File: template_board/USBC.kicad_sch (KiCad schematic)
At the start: 13 parts, among them J1 USB_C_Receptacle_USB2.0_16P, U1 IP4220CZ6, U11 FSUSB42UMX, U3 IP4220CZ6

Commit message: chamt skończony chyba
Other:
- moved on the sheet: C44, C45, C46, J1, R56, R57, R58, R59, R60, R61, U1, U11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

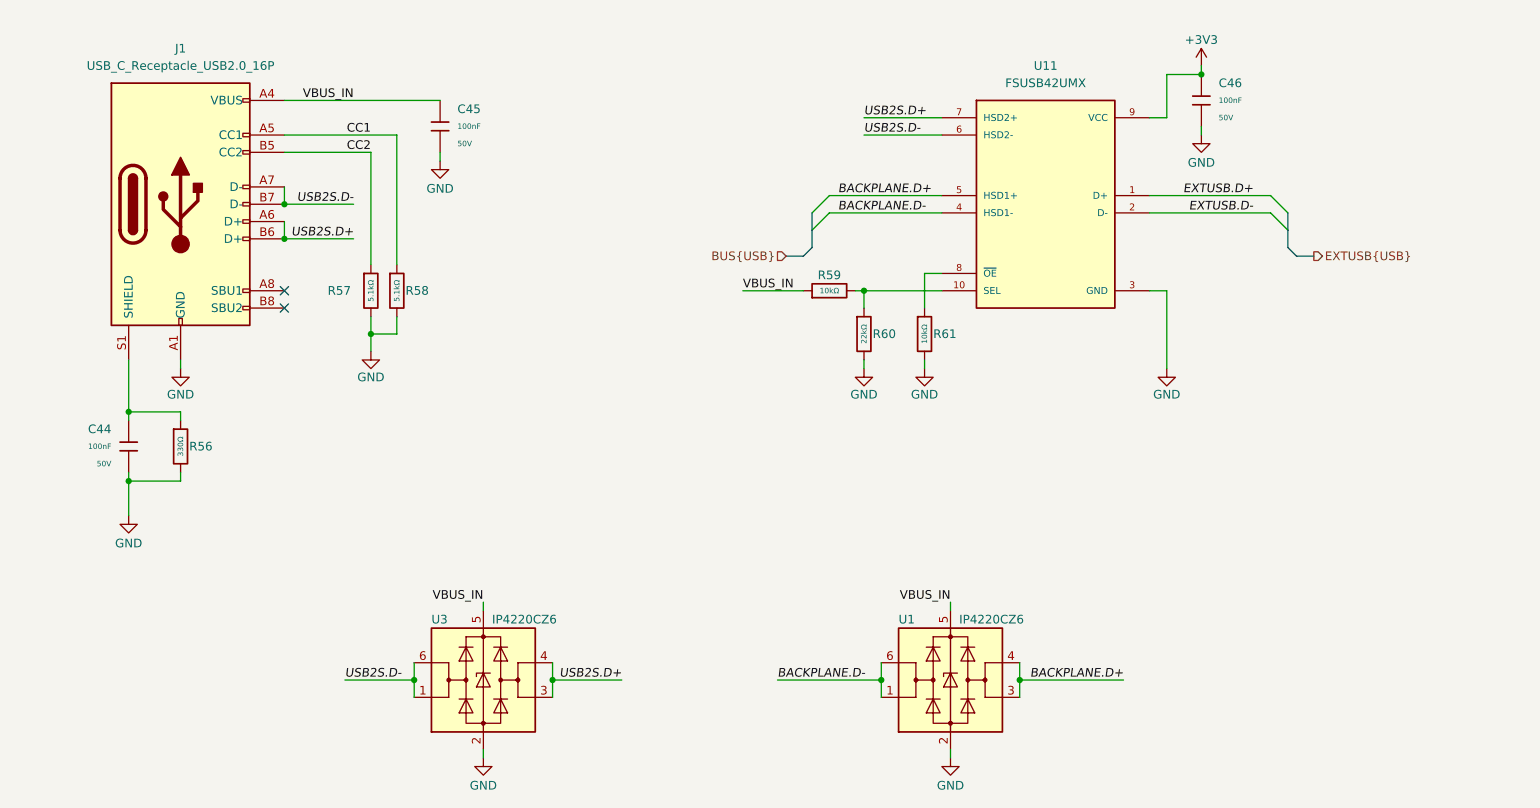
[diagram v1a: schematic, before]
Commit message: sub leyoyut partially completed
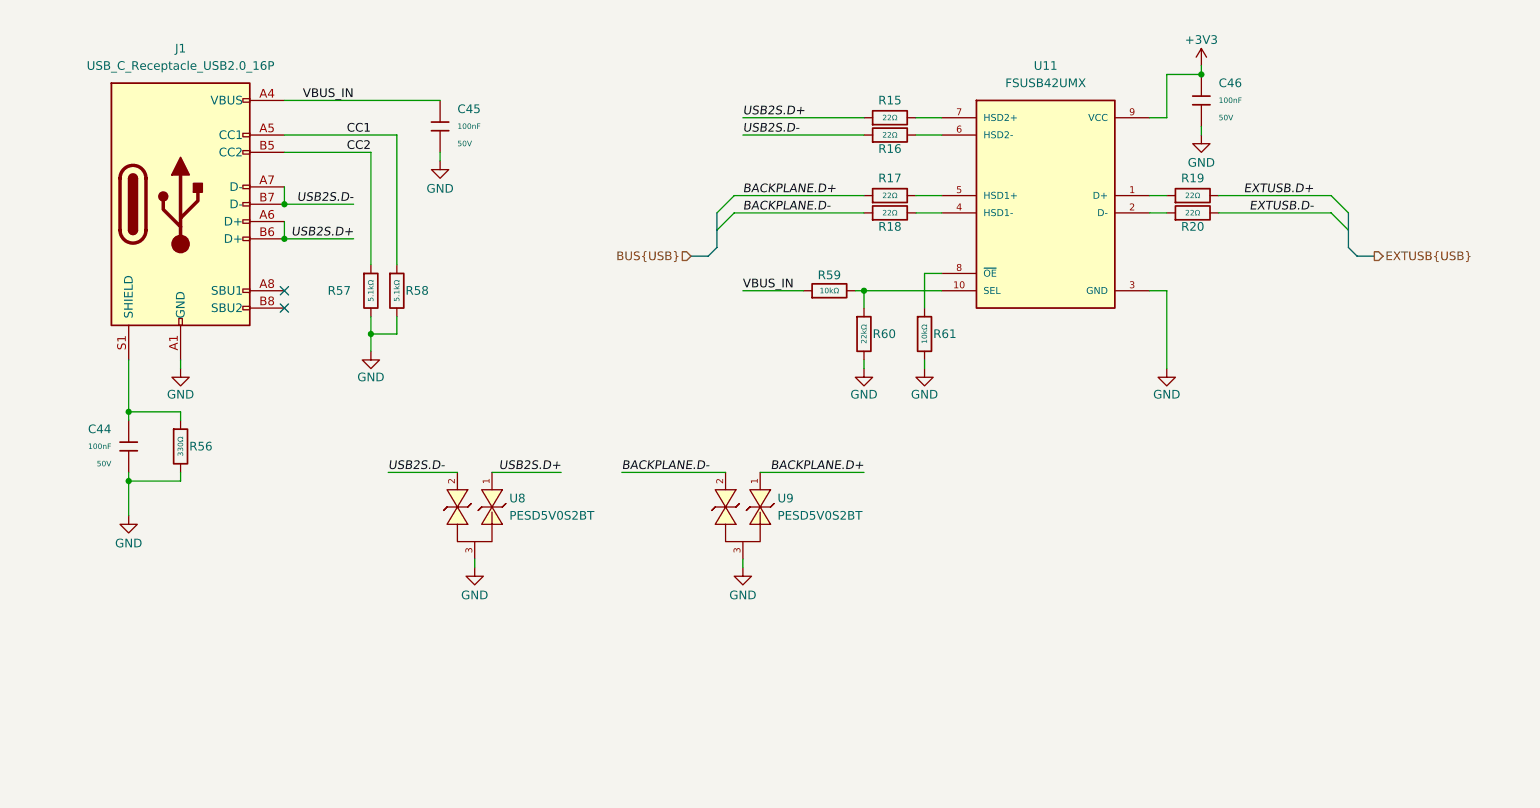
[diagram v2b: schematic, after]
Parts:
- removed U1, U3: IP4220CZ6, Package_TO_SOT_SMD:SOT-23-6, symbol Power_Protection:USBLC6-2SC6
- added R15, R16, R17, R18, R19, R20: 22Ω, PCM_JLCPCB:R_0402, symbol PCM_JLCPCB-Resistors:0402,22Ω
- added U8, U9: PESD5V0S2BT, Package_TO_SOT_SMD:SOT-23, symbol PESD5V0S2BT:PESD5V0S2BT
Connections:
- net BACKPLANE.D+: now also R17.1, U9.1; no longer U11.5 (HSD1+)
- net BACKPLANE.D-: now also R18.1, U9.2; no longer U11.4 (HSD1-)
- net EXTUSB.D+: now also R19.2; no longer U11.1 (D+)
- net EXTUSB.D-: now also R20.2; no longer U11.2 (D-)
- net GND: now also U8.3, U9.3
- net USB2S.D+: now also R15.1, U8.1; no longer U11.7 (HSD2+)
- net USB2S.D-: now also R16.1, U8.2; no longer U11.6 (HSD2-)
- new net: R15.2, U11.7 (HSD2+)
- new net: R17.2, U11.5 (HSD1+)
- new net: R16.2, U11.6 (HSD2-)
- new net: R19.1, U11.1 (D+)
- new net: R20.1, U11.2 (D-)
- new net: R18.2, U11.4 (HSD1-)

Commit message: [schematics] fixed issue with: stlink->crystal capacitors, usb-> esd with too big capacitance, tranzistor for stlink-usb renum changed
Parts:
- removed U8, U9: PESD5V0S2BT, Package_TO_SOT_SMD:SOT-23, symbol PESD5V0S2BT:PESD5V0S2BT
- added U1, U3: IP4220CZ6, Package_TO_SOT_SMD:SOT-23-6, symbol Power_Protection:USBLC6-2SC6
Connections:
- net GND: now also U1.2 (GND), U3.2 (GND)
- net USB2S.D+: now also U1.3 (I/O2), U1.4 (I/O2)
- net USB2S.D-: now also U1.1 (I/O1), U1.6 (I/O1)
- net VBUS_IN: now also U1.5 (VBUS)
- net BACKPLANE.D+ renamed BUS.D+
- net BUS.D+: now also U3.3 (I/O2), U3.4 (I/O2)
- net BACKPLANE.D- renamed BUS.D-
- net BUS.D-: now also U3.1 (I/O1), U3.6 (I/O1)
- new net +5V: U3.5 (VBUS)
